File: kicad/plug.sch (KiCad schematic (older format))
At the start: 2 parts, among them J1 74320-1004, P1 HDMI_RECEPTACLE

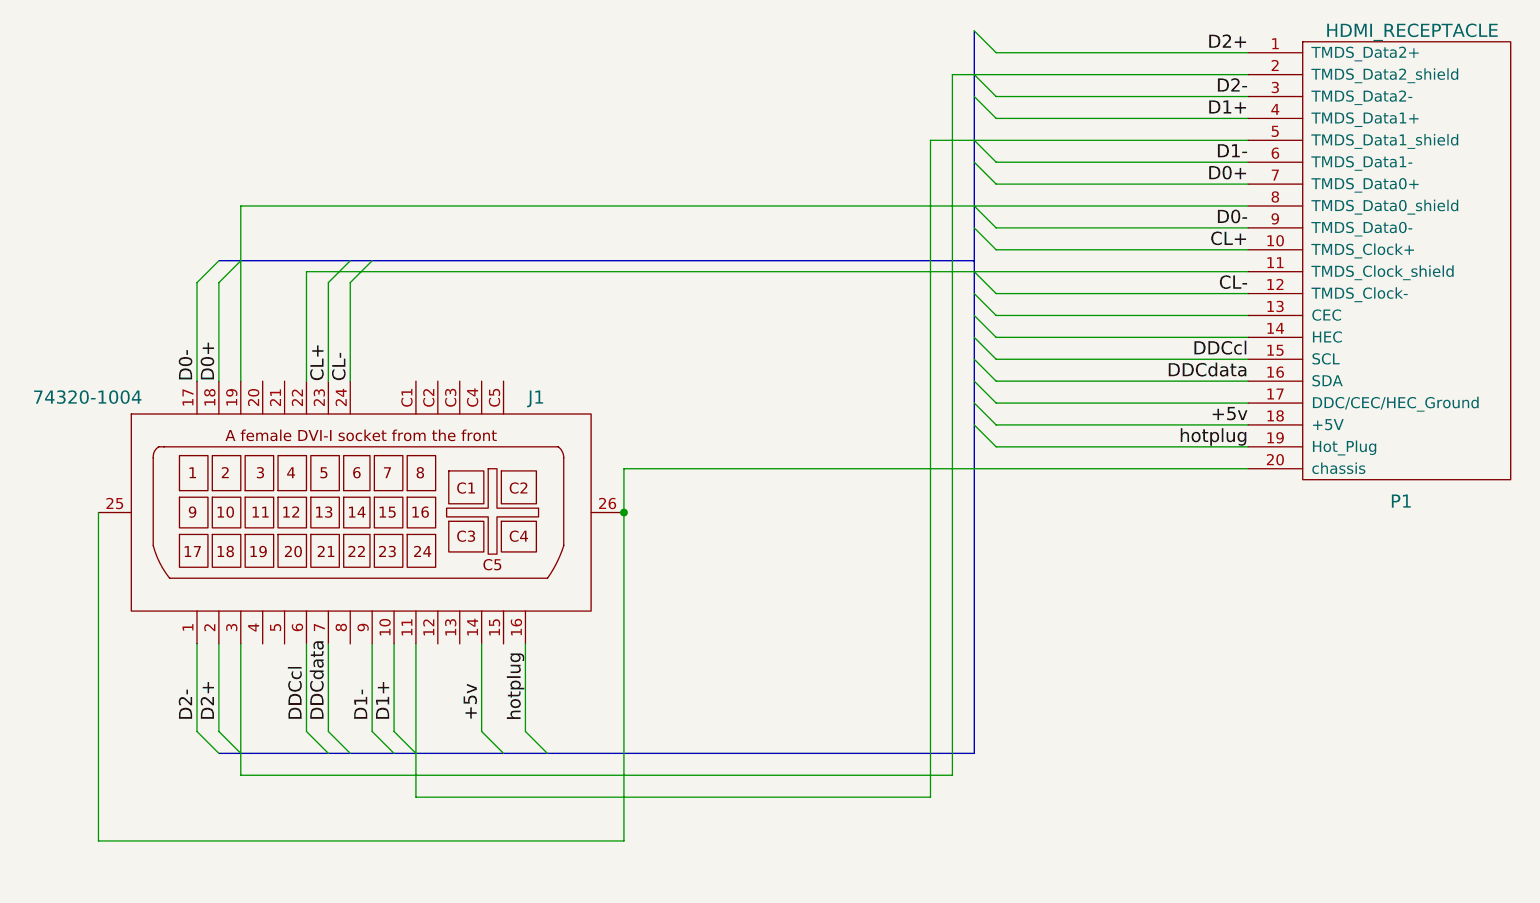
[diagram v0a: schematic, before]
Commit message: changed HDMI socket for SMD footprint + rewiring + all shields connected to ground
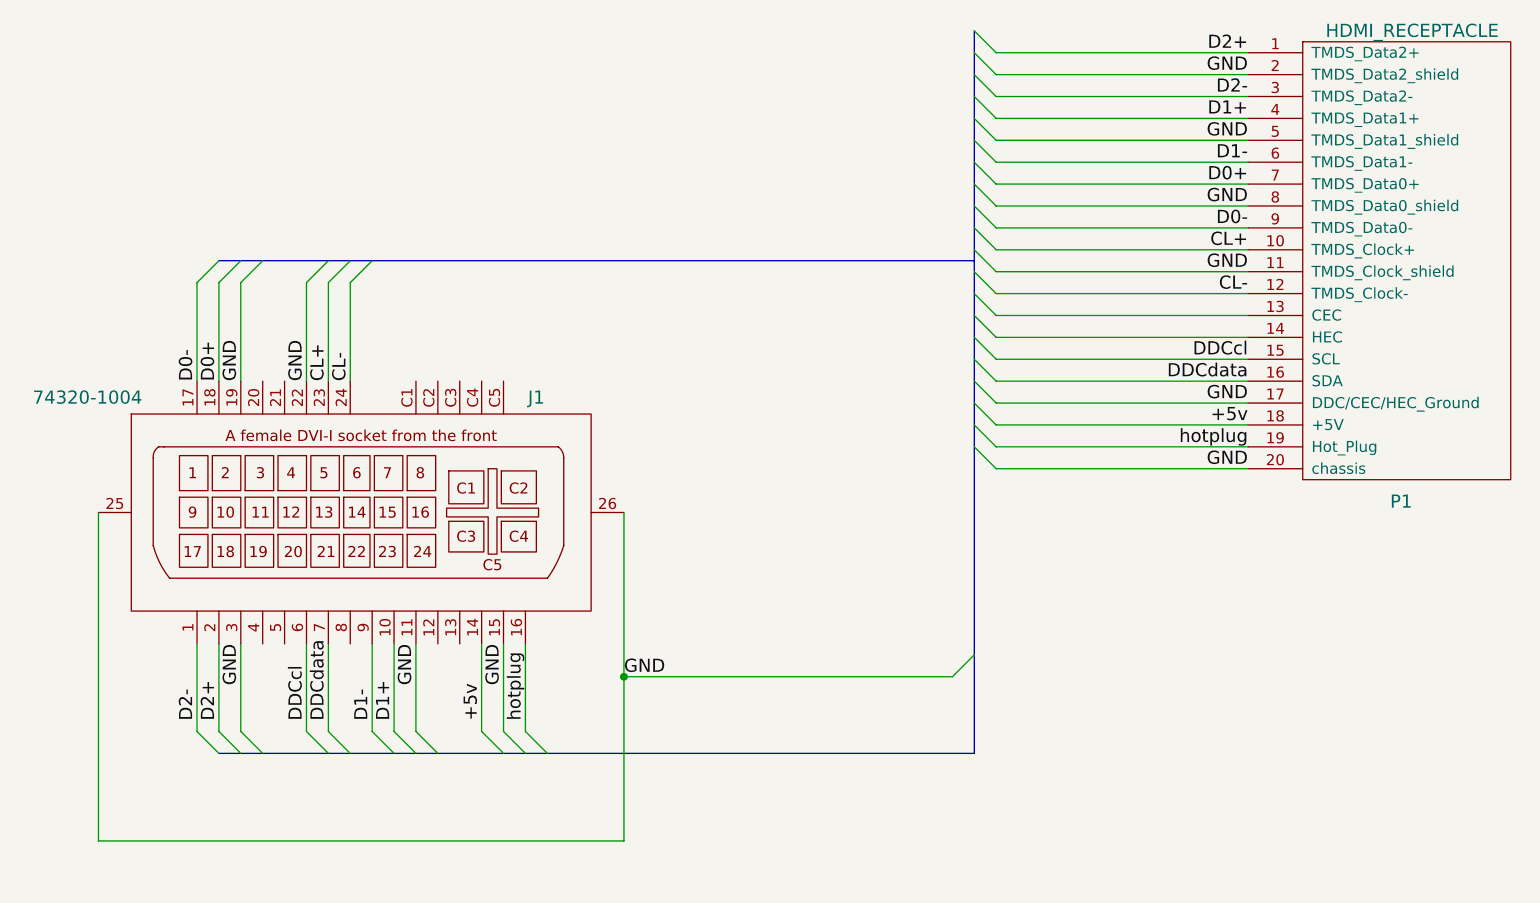
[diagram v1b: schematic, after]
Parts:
- J1: footprint (none) -> project:DVI-RECEPT-RA-HDMI
- P1: footprint HDMI:HDMI -> project:HDMI_SMD
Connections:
- net GND: now reaches J1.11 (TMDS_Data_1/3_shield), P1.5 (TMDS_Data1_shield)
- net GND: now also J1.15 (Ground), J1.19 (TMDS_data_0/5_shield), J1.22 (TMDS_clock_shield), J1.25 (SHIELD), J1.26 (SHIELD), J1.3 (TMDS_Data_2/4_shield), P1.11 (TMDS_Clock_shield), P1.17 (DDC/CEC/HEC_Ground), P1.2 (TMDS_Data2_shield), P1.20 (chassis), P1.8 (TMDS_Data0_shield)
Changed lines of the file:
@@
 Comment4 ""
 $EndDescr
-Wire Wire Line
-	4650 3100 4650 3600
-Wire Wire Line
-	8950 3100 4650 3100
-Wire Wire Line
-	5150 4800 5150 5500
-Wire Wire Line
-	5150 5500 7500 5500
-Wire Wire Line
-	7500 5500 7500 2500
-Wire Wire Line
-	7500 2500 8950 2500
-Connection ~ 6100 4200
-Wire Wire Line
-	6100 5700 6100 4000
-Wire Wire Line
-	6100 5700 3700 5700
-Wire Wire Line
-	3700 5700 3700 4200
-Wire Bus Line
-	4250 3050 7700 3050
-Wire Wire Line
-	8950 3900 7800 3900
-Wire Wire Line
-	8950 3800 7800 3800
-Wire Wire Line
-	8950 3700 7800 3700
-Wire Wire Line
-	8950 3600 7800 3600
-Wire Wire Line
-	8950 3500 7800 3500
-Wire Wire Line
-	8950 3400 7800 3400
-Wire Wire Line
-	8950 3300 7800 3300
-Wire Wire Line
-	8950 3200 7800 3200
-Wire Wire Line
-	8950 3000 7800 3000
-Wire Wire Line
-	8950 2900 7800 2900
-Wire Wire Line
-	8950 2700 7800 2700
-Wire Wire Line
-	8950 2600 7800 2600
-Wire Wire Line
-	8950 2400 7800 2400
-Wire Wire Line
-	8950 2300 7800 2300
-Wire Wire Line
-	4750 4800 4750 5200
-Wire Wire Line
-	5650 4800 5650 5200
-Wire Wire Line
-	4150 3600 4150 3150
-Wire Wire Line
-	4950 5200 4950 4800
-Wire Wire Line
-	4750 3600 4750 3150
-Wire Wire Line
-	4150 5200 4150 4800
-Wire Wire Line
-	7800 2100 8950 2100
-Wire Wire Line
-	4250 4800 4250 5200
-Wire Wire Line
-	4850 3600 4850 3150
-Wire Wire Line
-	5050 4800 5050 5200
-Wire Wire Line
-	4250 3600 4250 3150
-Wire Wire Line
-	4650 4800 4650 5200
-Wire Wire Line
-	5450 4800 5450 5200
-Wire Bus Line
-	7700 2000 7700 5300
-Wire Bus Line
-	7700 5300 4250 5300
-Wire Wire Line
-	6100 4000 8950 4000
-Wire Wire Line
-	4350 4800 4350 5400
-Wire Wire Line
-	4350 5400 7600 5400
-Wire Wire Line
-	7600 5400 7600 2200
-Wire Wire Line
-	7600 2200 8950 2200
-Wire Wire Line
-	8950 2800 4350 2800
-Wire Wire Line
-	4350 2800 4350 3600
 Text Label 8950 3900 2    60   ~ 0
 hotplug
@@
 F 0 "P1" H 9650 1950 60  0000 C CNN
 F 1 "HDMI_RECEPTACLE" H 9700 4100 60  0000 C CNN
-F 2 "HDMI:HDMI" H 9650 3050 60  0001 C CNN
+F 2 "project:HDMI_SMD" H 9650 3050 60  0001 C CNN
 F 3 "" H 9650 3050 60  0001 C CNN
 	1    9650 3050
@@
 F 0 "J1" H 5700 4725 60  0000 C CNN
 F 1 "74320-1004" H 3650 4725 60  0000 C CNN
-F 2 "" H 5250 4200 60  0001 C CNN
+F 2 "project:DVI-RECEPT-RA-HDMI" H 5250 4200 60  0001 C CNN
 F 3 "" H 5250 4200 60  0001 C CNN
 	1    5250 4200
 	1    0    0    -1
 $EndComp
+Entry Wire Line
+	4350 3150 4450 3050
+Text Label 4350 3600 1    60   ~ 0
+GND
+Entry Wire Line
+	7700 2700 7800 2800
+Text Label 8950 2800 2    60   ~ 0
+GND
+Entry Wire Line
+	7700 3000 7800 3100
+Text Label 8950 3100 2    60   ~ 0
+GND
+Wire Wire Line
+	6100 5700 3700 5700
+Wire Wire Line
+	3700 5700 3700 4200
+Wire Bus Line
+	4250 3050 7700 3050
+Wire Wire Line
+	8950 3900 7800 3900
+Wire Wire Line
+	8950 3800 7800 3800
+Wire Wire Line
+	8950 3700 7800 3700
+Wire Wire Line
+	8950 3600 7800 3600
+Wire Wire Line
+	8950 3500 7800 3500
+Wire Wire Line
+	8950 3400 7800 3400
+Wire Wire Line
+	8950 3300 7800 3300
+Wire Wire Line
+	8950 3200 7800 3200
+Wire Wire Line
+	8950 3000 7800 3000
+Wire Wire Line
+	8950 2900 7800 2900
+Wire Wire Line
+	8950 2700 7800 2700
+Wire Wire Line
+	8950 2600 7800 2600
+Wire Wire Line
+	8950 2400 7800 2400
+Wire Wire Line
+	8950 2300 7800 2300
+Wire Wire Line
+	4750 4800 4750 5200
+Wire Wire Line
+	5650 4800 5650 5200
+Wire Wire Line
+	4150 3600 4150 3150
+Wire Wire Line
+	4950 5200 4950 4800
+Wire Wire Line
+	4750 3600 4750 3150
+Wire Wire Line
+	4150 5200 4150 4800
+Wire Wire Line
+	7800 2100 8950 2100
+Wire Wire Line
+	4250 4800 4250 5200
+Wire Wire Line
+	4850 3600 4850 3150
+Wire Wire Line
+	5050 4800 5050 5200
+Wire Wire Line
+	4650 4800 4650 5200
+Wire Wire Line
+	5450 4800 5450 5200
+Wire Bus Line
+	7700 5300 7700 2000
+Wire Bus Line
+	4250 5300 7700 5300
+Wire Wire Line
+	7700 2800 7700 2800
+Wire Wire Line
+	4250 3600 4250 3150
+Wire Wire Line
+	4350 3600 4350 3150
+Wire Wire Line
+	7800 2800 8950 2800
+Wire Wire Line
+	7800 3100 8950 3100
+Wire Wire Line
+	4650 3600 4650 3150
+Entry Wire Line
+	4650 3150 4750 3050
+Text Label 4650 3600 1    60   ~ 0
+GND
+Wire Wire Line
+	4350 4800 4350 5200
+Entry Wire Line
+	4350 5200 4450 5300
+Text Label 4350 4800 3    60   ~ 0
+GND
+Wire Wire Line
+	8950 2200 7800 2200
+Entry Wire Line
+	7700 2100 7800 2200
+Text Label 8950 2200 2    60   ~ 0
+GND
+Wire Wire Line
+	5150 4800 5150 5200
+Entry Wire Line
+	5150 5200 5250 5300
+Text Label 5150 4800 3    60   ~ 0
+GND
+Wire Wire Line
+	8950 2500 7800 2500
+Entry Wire Line
+	7700 2400 7800 2500
+Text Label 8950 2500 2    60   ~ 0
+GND
+Entry Wire Line
+	7600 4950 7700 4850
+Wire Wire Line
+	6100 4200 6100 5700
+Wire Wire Line
+	7600 4950 6100 4950
+Connection ~ 6100 4950
+Text Label 6100 4950 0    60   ~ 0
+GND
+Entry Wire Line
+	7700 3900 7800 4000
+Wire Wire Line
+	7800 4000 8950 4000
+Text Label 8950 4000 2    60   ~ 0
+GND
+Text Label 8950 3700 2    60   ~ 0
+GND
+Entry Wire Line
+	5550 5200 5650 5300
+Wire Wire Line
+	5550 4800 5550 5200
+Text Label 5550 4800 3    60   ~ 0
+GND
 $EndSCHEMATC

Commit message: simplier version since hdmi is a pain to manage.
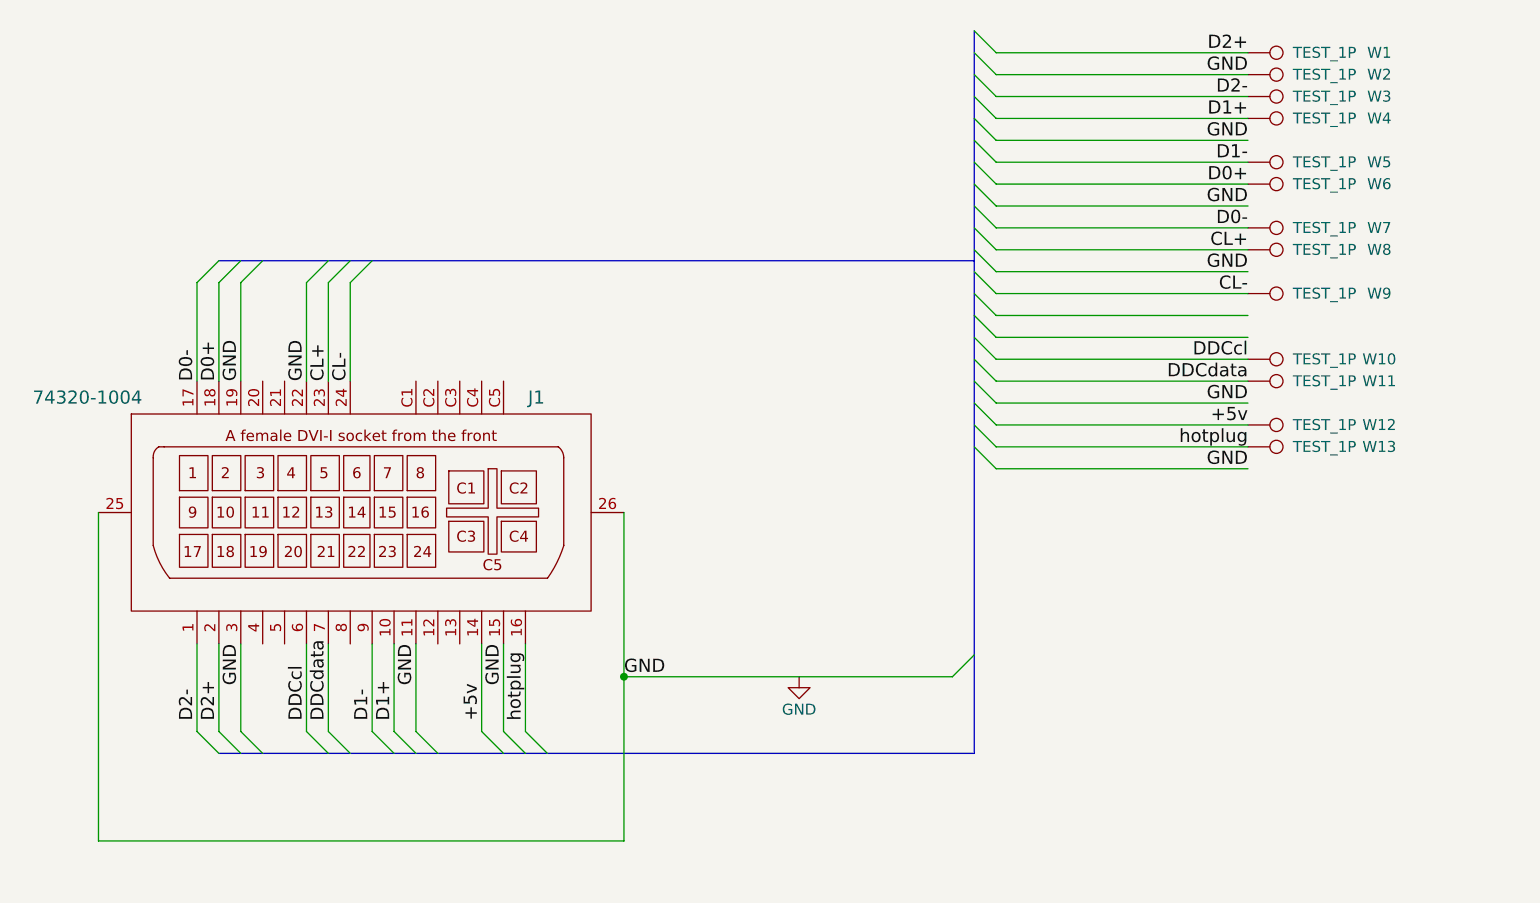
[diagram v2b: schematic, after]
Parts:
- removed P1: HDMI_RECEPTACLE, project:HDMI_SMD, symbol HDMI_RECEPTACLE
- added W1, W10, W11, W12, W13, W2, W3, W4, W5, W6, W7, W8, W9: TEST_1P, Connectors:PINTST, symbol TEST_1P
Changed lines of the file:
@@
 EESchema Schematic File Version 2
 LIBS:power
+LIBS:device
+LIBS:transistors
+LIBS:conn
+LIBS:linear
+LIBS:regul
+LIBS:74xx
+LIBS:cmos4000
+LIBS:adc-dac
+LIBS:memory
+LIBS:xilinx
+LIBS:microcontrollers
+LIBS:dsp
+LIBS:microchip
+LIBS:analog_switches
+LIBS:motorola
+LIBS:texas
+LIBS:intel
+LIBS:audio
+LIBS:interface
+LIBS:digital-audio
+LIBS:philips
+LIBS:display
+LIBS:cypress
+LIBS:siliconi
+LIBS:opto
+LIBS:atmel
+LIBS:contrib
+LIBS:valves
 LIBS:plug-cache
 EELAYER 25 0
@@
 D2-
 $Comp
-L HDMI_RECEPTACLE P1
-U 1 1 554F9844
-P 9650 3050
-F 0 "P1" H 9650 1950 60  0000 C CNN
-F 1 "HDMI_RECEPTACLE" H 9700 4100 60  0000 C CNN
-F 2 "project:HDMI_SMD" H 9650 3050 60  0001 C CNN
-F 3 "" H 9650 3050 60  0001 C CNN
-	1    9650 3050
-	1    0    0    -1
-$EndComp
-$Comp
 L 74320-1004 J1
 U 1 1 551899AA
@@
 Text Label 5550 4800 3    60   ~ 0
 GND
+$Comp
+L TEST_1P W1
+U 1 1 585599FC
+P 8950 2100
+F 0 "W1" V 8950 2700 50  0000 C CNN
+F 1 "TEST_1P" V 8950 2450 50  0000 C CNN
+F 2 "Connectors:PINTST" H 9150 2100 50  0001 C CNN
+F 3 "" H 9150 2100 50  0000 C CNN
+	1    8950 2100
+	0    1    1    0
+$EndComp
+$Comp
+L TEST_1P W2
+U 1 1 5855A0B8
+P 8950 2200
+F 0 "W2" V 8950 2800 50  0000 C CNN
+F 1 "TEST_1P" V 8950 2550 50  0000 C CNN
+F 2 "Connectors:PINTST" H 9150 2200 50  0001 C CNN
+F 3 "" H 9150 2200 50  0000 C CNN
+	1    8950 2200
+	0    1    1    0
+$EndComp
+$Comp
+L TEST_1P W3
+U 1 1 5855A0D1
+P 8950 2300
+F 0 "W3" V 8950 2900 50  0000 C CNN
+F 1 "TEST_1P" V 8950 2650 50  0000 C CNN
+F 2 "Connectors:PINTST" H 9150 2300 50  0001 C CNN
+F 3 "" H 9150 2300 50  0000 C CNN
+	1    8950 2300
+	0    1    1    0
+$EndComp
+$Comp
+L TEST_1P W4
+U 1 1 5855A0ED
+P 8950 2400
+F 0 "W4" V 8950 3000 50  0000 C CNN
+F 1 "TEST_1P" V 8950 2750 50  0000 C CNN
+F 2 "Connectors:PINTST" H 9150 2400 50  0001 C CNN
+F 3 "" H 9150 2400 50  0000 C CNN
+	1    8950 2400
+	0    1    1    0
+$EndComp
+$Comp
+L TEST_1P W5
+U 1 1 5855A10C
+P 8950 2600
+F 0 "W5" V 8950 3200 50  0000 C CNN
+F 1 "TEST_1P" V 8950 2950 50  0000 C CNN
+F 2 "Connectors:PINTST" H 9150 2600 50  0001 C CNN
+F 3 "" H 9150 2600 50  0000 C CNN
+	1    8950 2600
+	0    1    1    0
+$EndComp
+$Comp
+L TEST_1P W6
+U 1 1 5855A146
+P 8950 2700
+F 0 "W6" V 8950 3300 50  0000 C CNN
+F 1 "TEST_1P" V 8950 3050 50  0000 C CNN
+F 2 "Connectors:PINTST" H 9150 2700 50  0001 C CNN
+F 3 "" H 9150 2700 50  0000 C CNN
+	1    8950 2700
+	0    1    1    0
+$EndComp
+$Comp
+L TEST_1P W7
+U 1 1 5855A177
+P 8950 2900
+F 0 "W7" V 8950 3500 50  0000 C CNN
+F 1 "TEST_1P" V 8950 3250 50  0000 C CNN
+F 2 "Connectors:PINTST" H 9150 2900 50  0001 C CNN
+F 3 "" H 9150 2900 50  0000 C CNN
+	1    8950 2900
+	0    1    1    0
+$EndComp
+$Comp
+L TEST_1P W8
+U 1 1 5855A1A7
+P 8950 3000
+F 0 "W8" V 8950 3600 50  0000 C CNN
+F 1 "TEST_1P" V 8950 3350 50  0000 C CNN
+F 2 "Connectors:PINTST" H 9150 3000 50  0001 C CNN
+F 3 "" H 9150 3000 50  0000 C CNN
+	1    8950 3000
+	0    1    1    0
+$EndComp
+$Comp
+L TEST_1P W9
+U 1 1 5855A1D2
+P 8950 3200
+F 0 "W9" V 8950 3800 50  0000 C CNN
+F 1 "TEST_1P" V 8950 3550 50  0000 C CNN
+F 2 "Connectors:PINTST" H 9150 3200 50  0001 C CNN
+F 3 "" H 9150 3200 50  0000 C CNN
+	1    8950 3200
+	0    1    1    0
+$EndComp
+$Comp
+L TEST_1P W10
+U 1 1 5855A204
+P 8950 3500
+F 0 "W10" V 8950 4100 50  0000 C CNN
+F 1 "TEST_1P" V 8950 3850 50  0000 C CNN
+F 2 "Connectors:PINTST" H 9150 3500 50  0001 C CNN
+F 3 "" H 9150 3500 50  0000 C CNN
+	1    8950 3500
+	0    1    1    0
+$EndComp
+$Comp
+L TEST_1P W11
+U 1 1 5855A241
+P 8950 3600
+F 0 "W11" V 8950 4200 50  0000 C CNN
+F 1 "TEST_1P" V 8950 3950 50  0000 C CNN
+F 2 "Connectors:PINTST" H 9150 3600 50  0001 C CNN
+F 3 "" H 9150 3600 50  0000 C CNN
+	1    8950 3600
+	0    1    1    0
+$EndComp
+$Comp
+L TEST_1P W12
+U 1 1 5855A275
+P 8950 3800
+F 0 "W12" V 8950 4400 50  0000 C CNN
+F 1 "TEST_1P" V 8950 4150 50  0000 C CNN
+F 2 "Connectors:PINTST" H 9150 3800 50  0001 C CNN
+F 3 "" H 9150 3800 50  0000 C CNN
+	1    8950 3800
+	0    1    1    0
+$EndComp
+$Comp
+L TEST_1P W13
+U 1 1 5855A312
+P 8950 3900
+F 0 "W13" V 8950 4500 50  0000 C CNN
+F 1 "TEST_1P" V 8950 4250 50  0000 C CNN
+F 2 "Connectors:PINTST" H 9150 3900 50  0001 C CNN
+F 3 "" H 9150 3900 50  0000 C CNN
+	1    8950 3900
+	0    1    1    0
+$EndComp
+$Comp
+L GND #PWR01
+U 1 1 5855A718
+P 6900 4950
+F 0 "#PWR01" H 6900 4700 50  0001 C CNN
+F 1 "GND" H 6900 4800 50  0000 C CNN
+F 2 "" H 6900 4950 50  0000 C CNN
+F 3 "" H 6900 4950 50  0000 C CNN
+	1    6900 4950
+	1    0    0    -1
+$EndComp
 $EndSCHEMATC
